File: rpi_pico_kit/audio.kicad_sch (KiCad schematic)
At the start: 36 parts, among them J10 AudioJack-CUI-SJ-3523-SMT, J11 AudioJack-CUI-SJ-3523-SMT, Q7 DMN63D8L-7, U7 NC7WZ16P6X, U8 PCM5101A, U9 TLV70033_SOT23-5

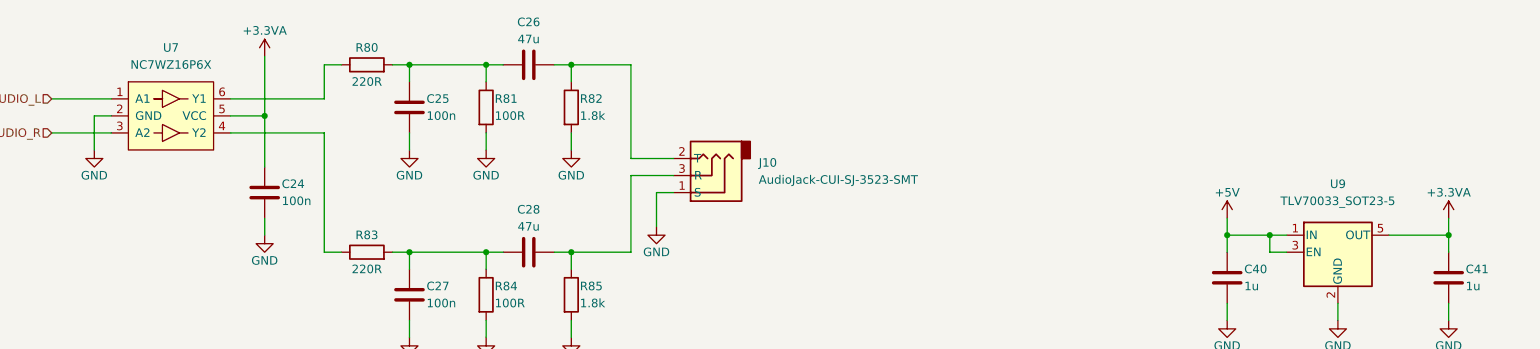
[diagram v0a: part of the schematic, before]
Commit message: added MPNs
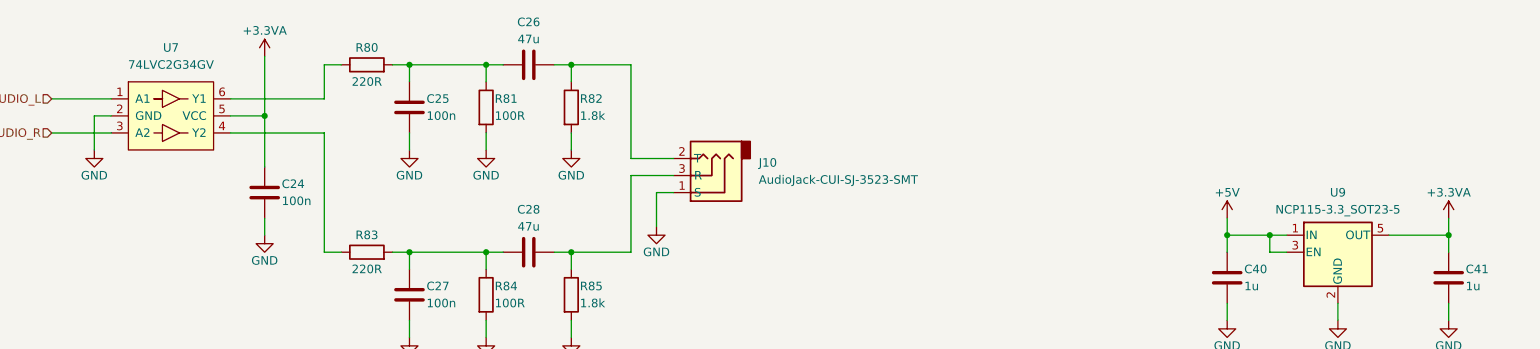
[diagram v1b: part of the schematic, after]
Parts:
- U7: value NC7WZ16P6X -> 74LVC2G34GV; footprint Package_TO_SOT_SMD:SOT-363_SC-70-6 -> Package_SO:SC-74-6_1.5x2.9mm_P0.95mm; Manufacturer Part Number (none) -> 74LVC2G34GV,125; Supplier (none) -> Digikey; Supplier Part URL (none) -> https://www.digikey.cz/en/products/detail/nexperia-usa-inc/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
- U9: value TLV70033_SOT23-5 -> NCP115-3.3_SOT23-5; Manufacturer Part Number (none) -> NCP115ASN330T2G; Supplier (none) -> Digikey; Supplier Part URL (none) -> https://www.digikey.cz/en/products/detail/onsemi/NCP115ASN3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
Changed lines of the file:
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@@
   (symbol (lib_id "Regulator_Linear:TLV70033_SOT23-5") (at 227.33 60.96 0) (unit 1)
     (in_bom yes) (on_board yes) (fields_autoplaced)
-    (property "Reference" "U9" (id 0) (at 227.33 50.8 0)
-      (effects (font (size 1.27 1.27)))
-    )
-    (property "Value" "TLV70033_SOT23-5" (id 1) (at 227.33 53.34 0)
+    (property "Reference" "U9" (id 0) (at 227.33 52.07 0)
+      (effects (font (size 1.27 1.27)))
+    )
+    (property "Value" "NCP115-3.3_SOT23-5" (id 1) (at 227.33 54.61 0)
       (effects (font (size 1.27 1.27)))
     )
@@
     )
     (property "Datasheet" "http://www.ti.com/lit/ds/symlink/tlv700.pdf" (id 3) (at 227.33 59.69 0)
+      (effects (font (size 1.27 1.27)) hide)
+    )
+    (property "Manufacturer Part Number" "NCP115ASN330T2G" (id 4) (at 227.33 60.96 0)
+      (effects (font (size 1.27 1.27)) hide)
+    )
+    (property "Supplier" "Digikey" (id 5) (at 227.33 60.96 0)
+      (effects (font (size 1.27 1.27)) hide)
+    )
+    (property "Supplier Part URL" "https://www.digikey.cz/en/products/detail/onsemi/NCP115ASN330T2G/9764776" (id 6) (at 227.33 60.96 0)
       (effects (font (size 1.27 1.27)) hide)
     )
@@
       (effects (font (size 1.27 1.27)))
     )
-    (property "Value" "NC7WZ16P6X" (id 1) (at 53.34 33.02 0)
-      (effects (font (size 1.27 1.27)))
-    )
-    (property "Footprint" "Package_TO_SOT_SMD:SOT-363_SC-70-6" (id 2) (at 53.34 49.53 0)
+    (property "Value" "74LVC2G34GV" (id 1) (at 53.34 33.02 0)
+      (effects (font (size 1.27 1.27)))
+    )
+    (property "Footprint" "Package_SO:SC-74-6_1.5x2.9mm_P0.95mm" (id 2) (at 53.34 49.53 0)
       (effects (font (size 1.27 1.27)) hide)
     )
@@
       (effects (font (size 1.27 1.27)) hide)
     )
+    (property "Manufacturer Part Number" "74LVC2G34GV,125" (id 4) (at 53.34 40.64 0)
+      (effects (font (size 1.27 1.27)) hide)
+    )
+    (property "Supplier" "Digikey" (id 5) (at 53.34 40.64 0)
+      (effects (font (size 1.27 1.27)) hide)
+    )
+    (property "Supplier Part URL" "https://www.digikey.cz/en/products/detail/nexperia-usa-inc/74LVC2G34GV-125/1231596" (id 6) (at 53.34 40.64 0)
+      (effects (font (size 1.27 1.27)) hide)
+    )

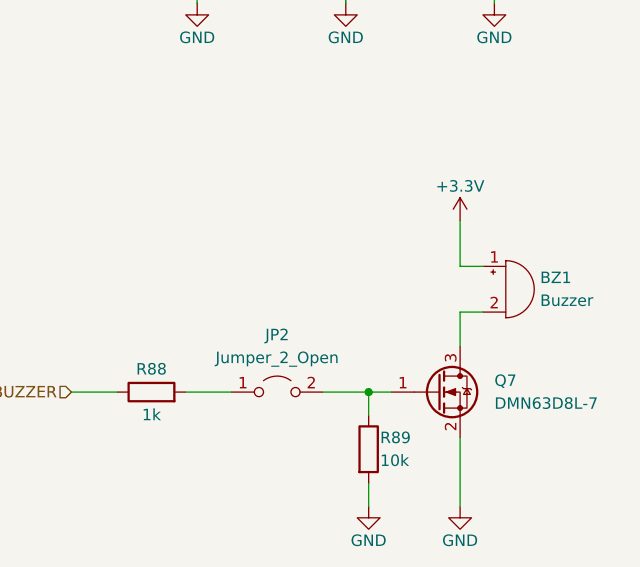
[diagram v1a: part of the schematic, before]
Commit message: added protective diode to buzzer
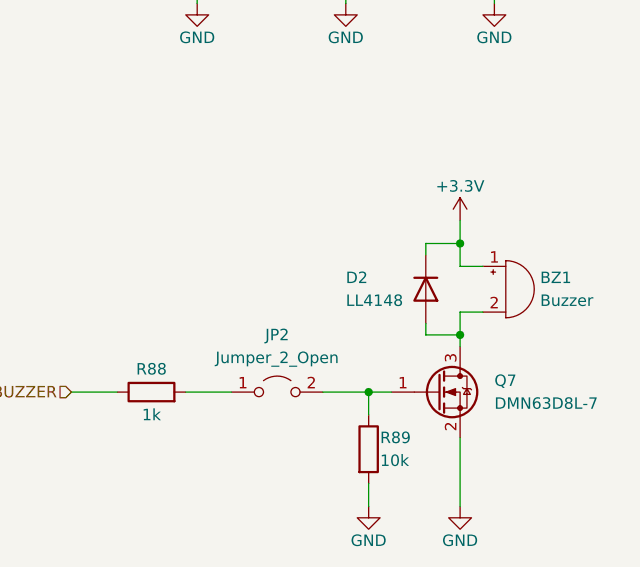
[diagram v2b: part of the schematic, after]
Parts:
- added D2: LL4148, Diode_SMD:D_MiniMELF, symbol Diode:LL4148
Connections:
- net +3V3: now also D2.1 (K)
- net at BZ1.2 (+), Q7.3 (D): now also D2.2 (A)
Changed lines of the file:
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@@
   (junction (at 69.85 109.22) (diameter 0) (color 0 0 0 0)
   )
+  (junction (at 240.03 97.79) (diameter 0) (color 0 0 0 0)
+  )
   (junction (at 46.99 109.22) (diameter 0) (color 0 0 0 0)
   )
@@
   (junction (at 72.39 161.29) (diameter 0) (color 0 0 0 0)
   )
+  (junction (at 240.03 107.95) (diameter 0) (color 0 0 0 0)
+  )
   (wire (pts (xy 100.33 43.18) (xy 100.33 45.72))
     (stroke (width 0) (type default))
@@
     (stroke (width 0) (type default))
   )
-  (wire (pts (xy 240.03 105.41) (xy 240.03 109.22))
+  (wire (pts (xy 240.03 105.41) (xy 240.03 107.95))
     (stroke (width 0) (type default))
   )
@@
     (stroke (width 0) (type default))
   )
+  (wire (pts (xy 236.22 97.79) (xy 240.03 97.79))
+    (stroke (width 0) (type default))
+  )
   (wire (pts (xy 86.36 109.22) (xy 86.36 111.76))
     (stroke (width 0) (type default))
@@
     (stroke (width 0) (type default))
   )
+  (wire (pts (xy 236.22 99.06) (xy 236.22 97.79))
+    (stroke (width 0) (type default))
+  )
   (wire (pts (xy 107.95 138.43) (xy 102.87 138.43))
     (stroke (width 0) (type default))
@@
     (stroke (width 0) (type default))
   )
-  (wire (pts (xy 240.03 100.33) (xy 240.03 95.25))
+  (wire (pts (xy 240.03 100.33) (xy 240.03 97.79))
     (stroke (width 0) (type default))
   )
@@
     (stroke (width 0) (type default))
   )
+  (wire (pts (xy 240.03 97.79) (xy 240.03 95.25))
+    (stroke (width 0) (type default))
+  )
   (wire (pts (xy 113.03 43.18) (xy 113.03 45.72))
     (stroke (width 0) (type default))
@@
     (stroke (width 0) (type default))
   )
+  (wire (pts (xy 236.22 107.95) (xy 240.03 107.95))
+    (stroke (width 0) (type default))
+  )
   (wire (pts (xy 85.09 132.08) (xy 95.25 132.08))
     (stroke (width 0) (type default))
@@
     (stroke (width 0) (type default))
   )
+  (wire (pts (xy 236.22 106.68) (xy 236.22 107.95))
+    (stroke (width 0) (type default))
+  )
   (wire (pts (xy 243.84 58.42) (xy 243.84 60.96))
     (stroke (width 0) (type default))
@@
   )
   (wire (pts (xy 90.17 138.43) (xy 95.25 138.43))
+    (stroke (width 0) (type default))
+  )
+  (wire (pts (xy 240.03 107.95) (xy 240.03 109.22))
     (stroke (width 0) (type default))
   )
@@
     (pin "1")
   )
+  (symbol (lib_id "Diode:LL4148") (at 236.22 102.87 270) (unit 1)
+    (in_bom yes) (on_board yes)
+    (property "Reference" "D2" (id 0) (at 227.33 101.6 90)
+      (effects (font (size 1.27 1.27)) (justify left))
+    )
+    (property "Value" "LL4148" (id 1) (at 227.33 104.14 90)
+      (effects (font (size 1.27 1.27)) (justify left))
+    )
+    (property "Footprint" "Diode_SMD:D_MiniMELF" (id 2) (at 231.775 102.87 0)
+      (effects (font (size 1.27 1.27)) hide)
+    )
+    (property "Datasheet" "http://www.vishay.com/docs/85557/ll4148.pdf" (id 3) (at 236.22 102.87 0)
+      (effects (font (size 1.27 1.27)) hide)
+    )
+    (property "Manufacturer Part Number" "LL4148" (id 4) (at 236.22 102.87 0)
+      (effects (font (size 1.27 1.27)) hide)
+    )
+    (property "Supplier" "Digikey" (id 5) (at 236.22 102.87 0)
+      (effects (font (size 1.27 1.27)) hide)
+    )
+    (property "Supplier Part URL" "https://www.digikey.cz/en/products/detail/onsemi/LL4148/1923046" (id 6) (at 236.22 102.87 0)
+      (effects (font (size 1.27 1.27)) hide)
+    )
+    (pin "1")
+    (pin "2")
+  )
   (symbol (lib_id "power:GND") (at 86.36 120.65 0) (unit 1)

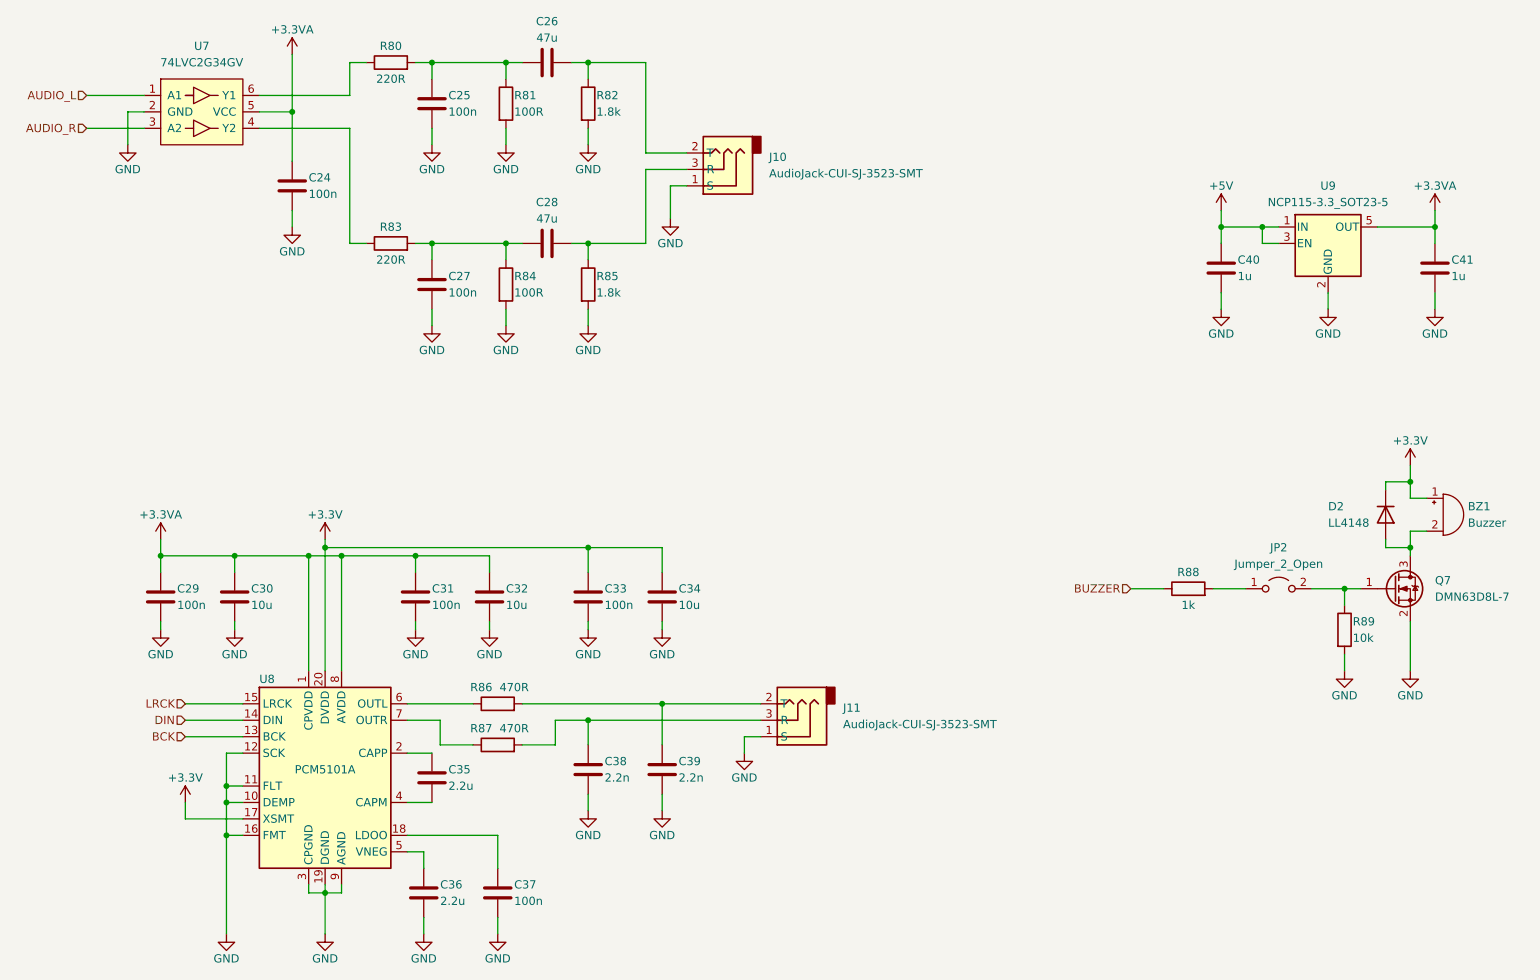
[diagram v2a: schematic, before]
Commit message: changed numbering of parts
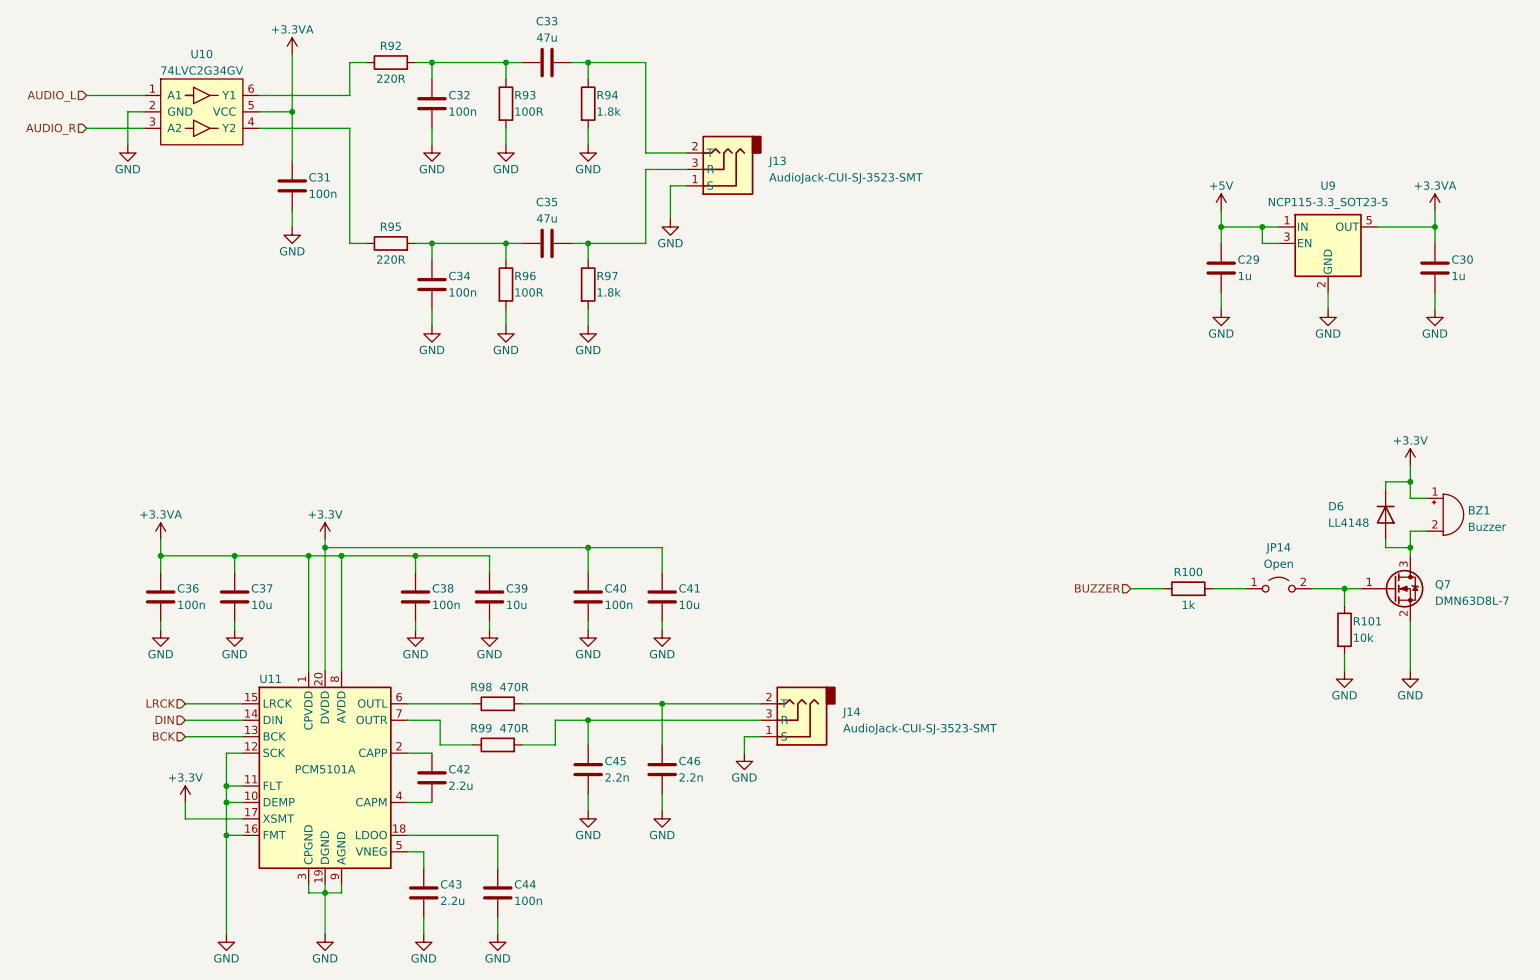
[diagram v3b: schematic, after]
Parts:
- JP14: renamed from JP2; value Jumper_2_Open -> Open
- renumbered C40 to C29, C41 to C30, C24 to C31, C25 to C32, C26 to C33, C27 to C34, C28 to C35, C29 to C36, C30 to C37, C31 to C38, C32 to C39, C33 to C40, C34 to C41, C35 to C42, C36 to C43, C37 to C44, C38 to C45, C39 to C46, D2 to D6, J10 to J13, J11 to J14, R88 to R100, R89 to R101, R80 to R92, R81 to R93, R82 to R94, R83 to R95, R84 to R96, R85 to R97, R86 to R98, R87 to R99, U7 to U10, U8 to U11
